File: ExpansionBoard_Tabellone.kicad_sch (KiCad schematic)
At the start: 31 parts, among them J101 LED, J102 RESET, J103 UART, J104 RELAY, J105 GPIO, J106 GPIO, J107 GPIO, J108 5V, J109 GND, J110 3V3, J111 GPIO, J112 RTC, J113 Conn_01x15, J114 Conn_01x15, J115 RELAY1, J116 RELAY2, J117 GPIO, K101 SANYOU_SRD_Form_C, K102 SANYOU_SRD_Form_C, Q101 BC337, Q102 BC337

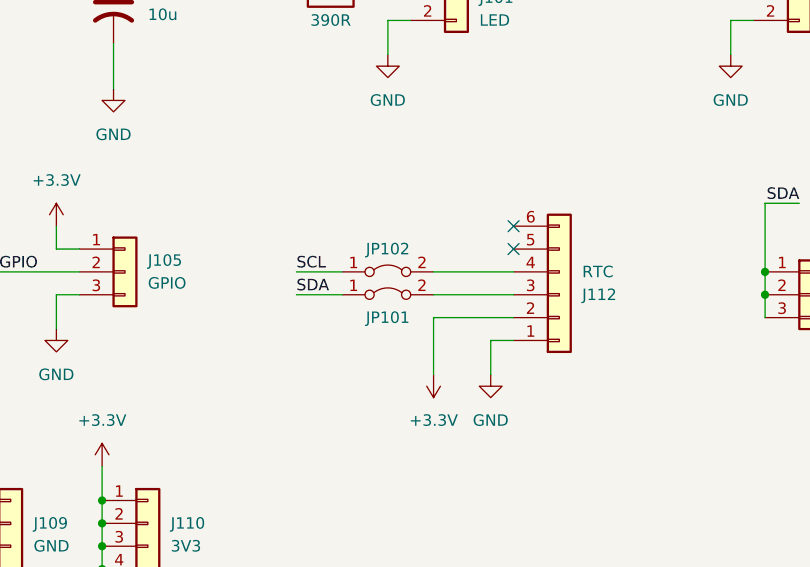
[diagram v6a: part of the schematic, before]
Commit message: Copletato anche il routing
Cambiato anche il morsetto del Rele1
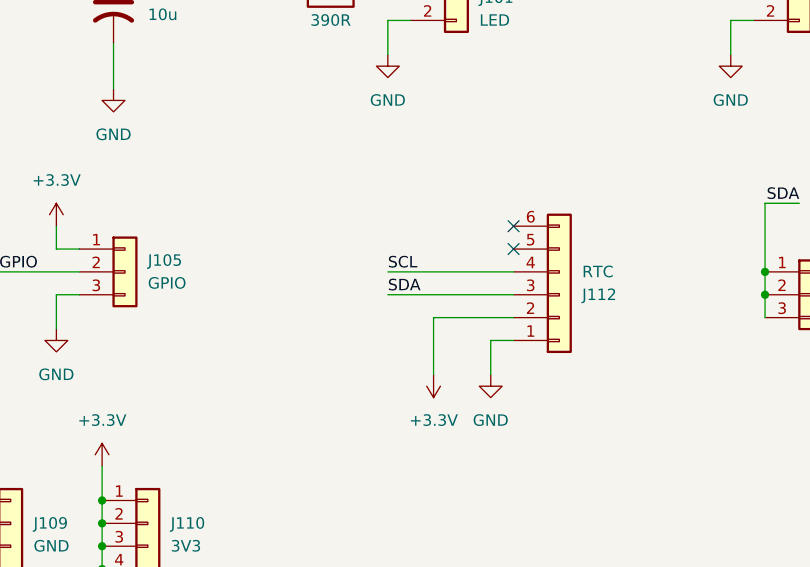
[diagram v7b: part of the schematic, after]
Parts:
- removed JP101, JP102: Jumper_2_Bridged, Jumper:SolderJumper-2_P1.3mm_Bridged_Pad1.0x1.5mm, symbol Jumper:Jumper_2_Bridged
- J115: footprint Connector_Header_P2.54_my:PinSocket_1x03_P2.54mm_Vertical_HandSoldering -> Connector_Screw_P5.08_my:ScrewConnector_1x03_P5.08mm_HandSoldering
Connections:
- net SCL: now also J112.4 (Pin_4)
- net SDA: now also J112.3 (Pin_3)
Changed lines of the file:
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@@
     (stroke (width 0) (type default))
   )
-  (wire (pts (xy 199.39 64.77) (xy 208.28 64.77))
+  (wire (pts (xy 194.31 64.77) (xy 208.28 64.77))
     (stroke (width 0) (type default))
   )
@@
     (stroke (width 0) (type default))
   )
-  (wire (pts (xy 184.15 67.31) (xy 189.23 67.31))
-    (stroke (width 0) (type default))
-  )
   (wire (pts (xy 93.98 60.96) (xy 101.6 60.96))
     (stroke (width 0) (type default))
@@
     (stroke (width 0) (type default))
   )
-  (wire (pts (xy 184.15 64.77) (xy 189.23 64.77))
-    (stroke (width 0) (type default))
-  )
   (wire (pts (xy 95.25 59.69) (xy 92.71 59.69))
     (stroke (width 0) (type default))
@@
     (stroke (width 0) (type default))
   )
-  (wire (pts (xy 199.39 67.31) (xy 208.28 67.31))
+  (wire (pts (xy 194.31 67.31) (xy 208.28 67.31))
     (stroke (width 0) (type default))
   )
@@
     (effects (font (size 1.27 1.27)) (justify left bottom))
   )
-  (label "SDA" (at 184.15 67.31 0) (fields_autoplaced)
+  (label "SDA" (at 194.31 67.31 0) (fields_autoplaced)
     (effects (font (size 1.27 1.27)) (justify left bottom))
   )
@@
     (effects (font (size 1.27 1.27)) (justify right bottom))
   )
-  (label "SCL" (at 184.15 64.77 0) (fields_autoplaced)
+  (label "SCL" (at 194.31 64.77 0) (fields_autoplaced)
     (effects (font (size 1.27 1.27)) (justify left bottom))
   )
@@
         (path "/ca8d62e8-a391-47e6-878e-b9b10e031484"
           (reference "J112") (unit 1)
-        )
-      )
-    )
-  )
-  (symbol (lib_id "Jumper:Jumper_2_Bridged") (at 194.31 64.77 0) (unit 1)
-    (in_bom yes) (on_board yes) (dnp no)
-    (property "Reference" "JP102" (at 194.31 62.23 0)
-      (effects (font (size 1.27 1.27)))
-    )
-    (property "Value" "Jumper_2_Bridged" (at 194.31 67.31 0)
-      (effects (font (size 1.27 1.27)) hide)
-    )
-    (property "Footprint" "Jumper:SolderJumper-2_P1.3mm_Bridged_Pad1.0x1.5mm" (at 194.31 64.77 0)
-      (effects (font (size 1.27 1.27)) hide)
-    )
-    (property "Datasheet" "~" (at 194.31 64.77 0)
-      (effects (font (size 1.27 1.27)) hide)
-    )
-    (pin "2")
-    (pin "1")
-    (instances
-      (project "ExpansionBoard_Tabellone"
-        (path "/ca8d62e8-a391-47e6-878e-b9b10e031484"
-          (reference "JP102") (unit 1)
         )
       )
@@
       (effects (font (size 1.27 1.27)) (justify left))
     )
-    (property "Footprint" "Connector_Header_P2.54_my:PinSocket_1x03_P2.54mm_Vertical_HandSoldering" (at 82.55 148.59 0)
+    (property "Footprint" "Connector_Screw_P5.08_my:ScrewConnector_1x03_P5.08mm_HandSoldering" (at 82.55 148.59 0)
       (effects (font (size 1.27 1.27)) hide)
     )
@@
         )
       )
-    )
-  )
-  (symbol (lib_id "Jumper:Jumper_2_Bridged") (at 194.31 67.31 0) (unit 1)
-    (in_bom yes) (on_board yes) (dnp no)
-    (property "Reference" "JP101" (at 194.31 69.85 0)
-      (effects (font (size 1.27 1.27)))
-    )
-    (property "Value" "Jumper_2_Bridged" (at 194.31 64.77 0)
-      (effects (font (size 1.27 1.27)) hide)
-    )
-    (property "Footprint" "Jumper:SolderJumper-2_P1.3mm_Bridged_Pad1.0x1.5mm" (at 194.31 67.31 0)
-      (effects (font (size 1.27 1.27)) hide)
-    )
-    (property "Datasheet" "~" (at 194.31 67.31 0)
-      (effects (font (size 1.27 1.27)) hide)
-    )
-    (pin "2")
-    (pin "1")
-    (instances
-      (project "ExpansionBoard_Tabellone"
-        (path "/ca8d62e8-a391-47e6-878e-b9b10e031484"
-          (reference "JP101") (unit 1)
-        )
-      )

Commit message: Ultime modifiche
 - Inserito connettore per relè
 - Compilati i cartigli
 - Ultimi fix
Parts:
- D102, J116, Q102, R103: now fitted
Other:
- company: (none) -> Alan Masutti
- title: (none) -> Espansion Board per Tabellone Segnapunti
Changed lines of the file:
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@@
 (kicad_sch (version 20230121) (generator eeschema)
   (paper "A4")
+  (title_block
+    (title "Espansion Board per Tabellone Segnapunti")
+    (date "2024-12-06")
+    (rev "1.0")
+    (company "Alan Masutti")
+  )
   (junction (at 43.18 140.97) (diameter 0) (color 0 0 0 0)
   )
@@
   )
   (symbol (lib_id "Transistor_BJT:BC337") (at 115.57 167.64 0) (unit 1)
-    (in_bom yes) (on_board yes) (dnp yes) (fields_autoplaced)
+    (in_bom yes) (on_board yes) (dnp no) (fields_autoplaced)
     (property "Reference" "Q102" (at 120.65 166.37 0)
       (effects (font (size 1.27 1.27)) (justify left))
@@
   )
   (symbol (lib_id "Diode:1N4148") (at 113.03 148.59 270) (unit 1)
-    (in_bom yes) (on_board yes) (dnp yes)
+    (in_bom yes) (on_board yes) (dnp no)
     (property "Reference" "D102" (at 102.87 147.32 90)
       (effects (font (size 1.27 1.27)) (justify left))
@@
   )
   (symbol (lib_id "Device:R") (at 104.14 167.64 270) (unit 1)
-    (in_bom yes) (on_board yes) (dnp yes)
+    (in_bom yes) (on_board yes) (dnp no)
     (property "Reference" "R103" (at 104.14 165.1 90)
       (effects (font (size 1.27 1.27)))
@@
   )
   (symbol (lib_id "Connector_Generic:Conn_01x03") (at 157.48 148.59 0) (unit 1)
-    (in_bom yes) (on_board yes) (dnp yes) (fields_autoplaced)
+    (in_bom yes) (on_board yes) (dnp no) (fields_autoplaced)
     (property "Reference" "J116" (at 160.02 147.32 0)
       (effects (font (size 1.27 1.27)) (justify left))
